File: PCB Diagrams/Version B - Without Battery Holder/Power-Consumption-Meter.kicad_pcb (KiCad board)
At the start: 2 copper layers, 90 x 96.5 mm, 35 parts, among them J1 Jack_DC, J10 01x02, J11 01x02, J12 01x02, J13 01x02, J2 01x02, J3 01x02, J4 USB_A, J5 Jack_DC, J6 Jack_DC, J7 USB_B_Mini, J8 USB_B_Micro, J9 01x04, SW1 SW_SPDT, SW2 SW_Push, U1 INA219_Module, U2 Display_5641BS

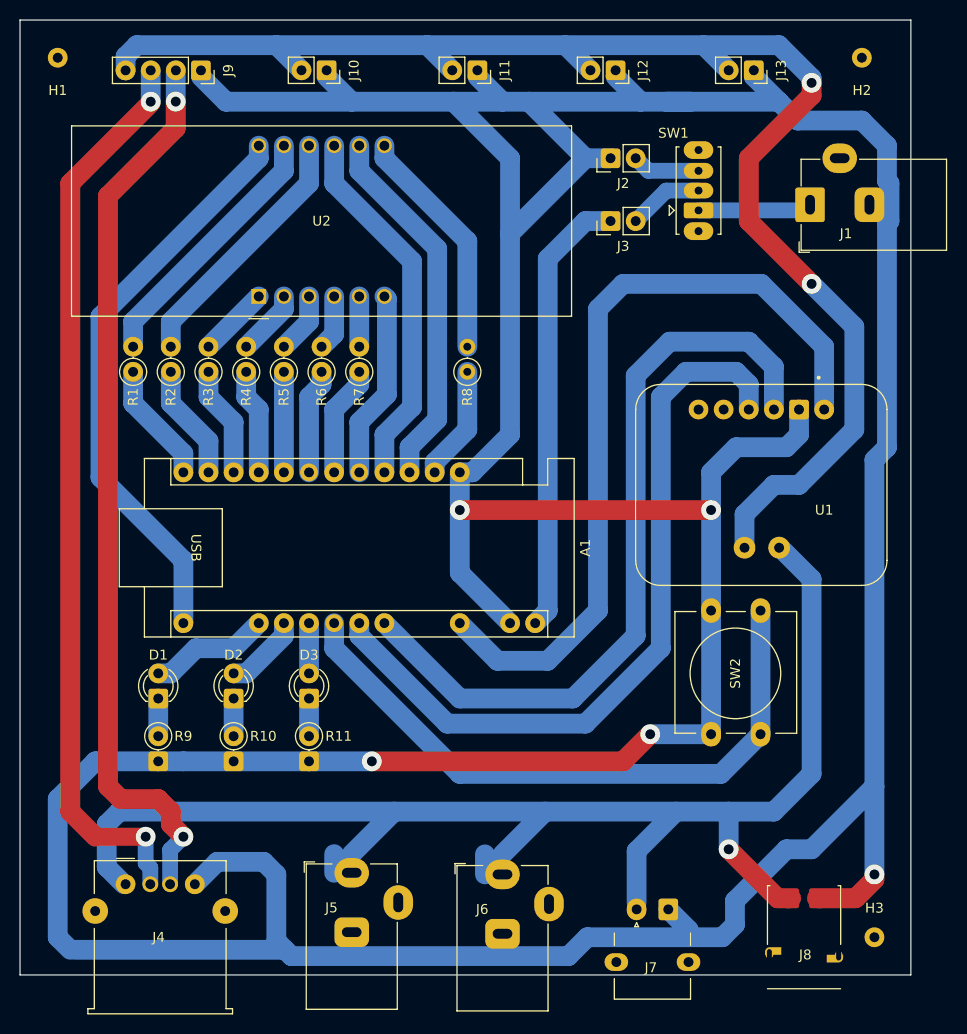
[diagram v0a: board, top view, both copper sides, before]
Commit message: update PCB connectors
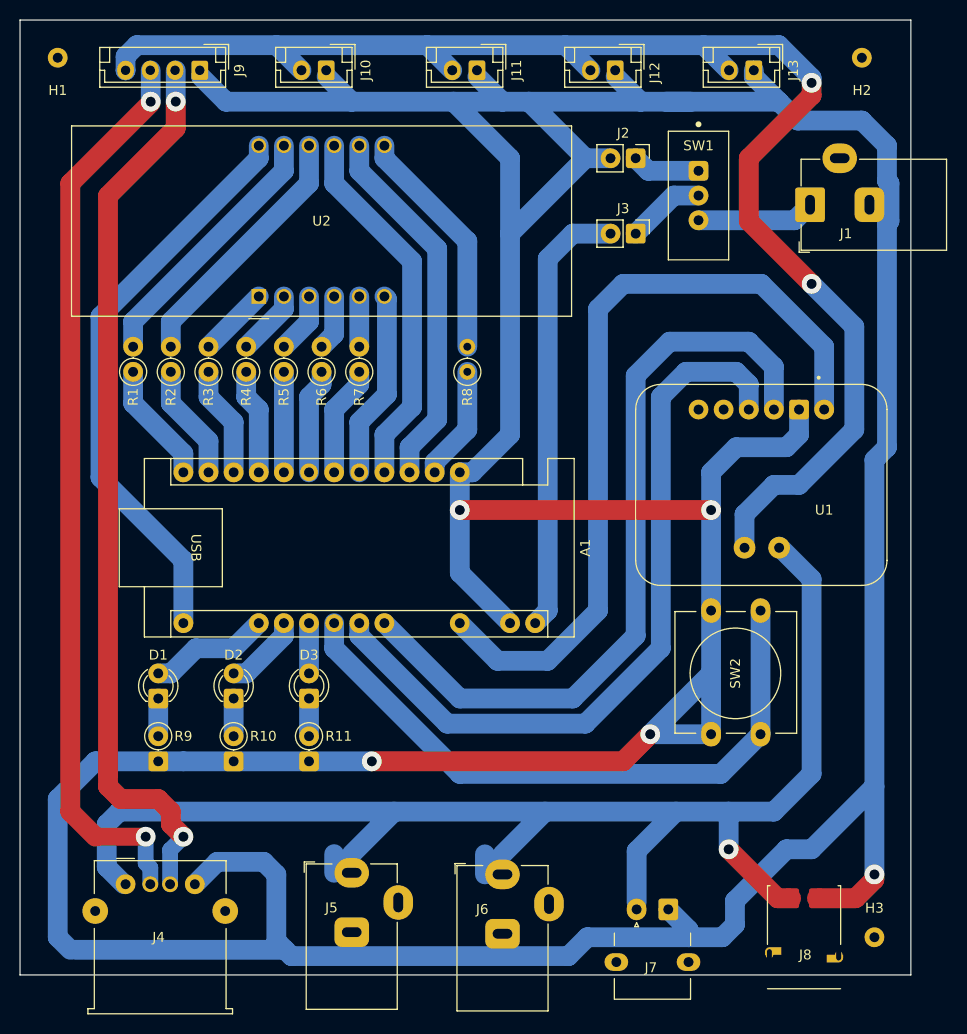
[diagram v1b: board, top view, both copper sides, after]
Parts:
- J10, J11, J12, J13: footprint Connector_PinSocket_2.54mm:PinSocket_1x02_P2.54mm_Vertical -> Connector_JST:JST_EH_B2B-EH-A_1x02_P2.50mm_Vertical
- J2: value 01x02 -> BAT_IN
- J3: value 01x02 -> PWR_BTN
- J9: footprint Connector_PinSocket_2.54mm:PinSocket_1x04_P2.54mm_Vertical -> Connector_JST:JST_EH_B4B-EH-A_1x04_P2.50mm_Vertical
- SW1: value SW_SPDT -> SW_Slide; footprint Button_Switch_THT:SW_Slide_SPDT_Straight_CK_OS102011MS2Q -> Custom:Switch_Slide_SPDT_Straight_TE_1825159_1
- moved J3 2.84 mm to (158.8, 54.6), turned to -90 degrees
- moved J2 2.54 mm to (158.7, 47.0), turned to -90 degrees
- moved SW1 1.50 mm to (165.1, 50.8), turned to -90 degrees
- moved J9 0.12 mm to (114.7, 38.1), turned to 180 degrees
- turned J10 to 180 degrees
- turned J11 to 180 degrees
- turned J12 to 180 degrees
- turned J13 to 180 degrees
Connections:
- J1 pad 1: Net-(SW1-A) -> Net-(J1-Pad1)
- J2 pad 1: GND -> Net-(J2-Pin_1)
- J2 pad 2: Net-(J2-Pin_2) -> GND
- J3 pad 1: PWR -> Net-(J3-Pin_1)
- J3 pad 2: Net-(J3-Pin_2) -> PWR
- SW1 pad 1: Net-(SW1-A) -> Net-(J2-Pin_1)
- SW1 pad 2: Net-(J3-Pin_2) -> Net-(J3-Pin_1)
- SW1 pad 3: Net-(J2-Pin_2) -> Net-(J1-Pad1)
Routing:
- net Net-(J1-Pad1): track 0.00 -> 11.9 mm
- net Net-(SW1-A): track 11.5 -> 0.00 mm
- net GND: track 513.0 -> 521.7 mm
- net Net-(J3-Pin_1): track 0.00 -> 7.94 mm
- net Net-(J3-Pin_2): track 7.63 -> 0.00 mm
- net Net-(J2-Pin_1): track 0.00 -> 6.88 mm
- net Net-(J2-Pin_2): track 6.88 -> 0.00 mm
- net PWR: track 45.3 -> 44.8 mm

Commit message: Adding PCB building and assembly pictures
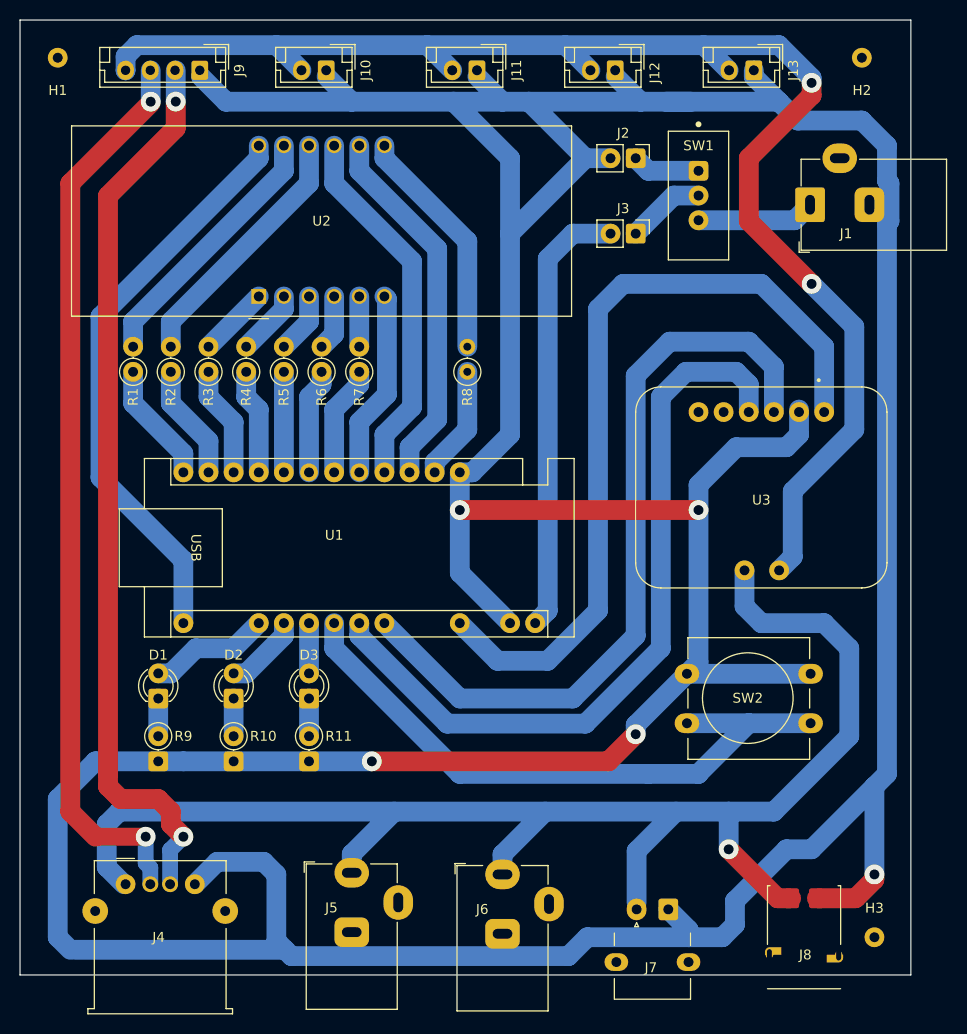
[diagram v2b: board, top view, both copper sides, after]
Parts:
- removed the U1 at (171.4, 80.0)
- added U3: INA219_Module, Custom:INA219_Module_Generic, F.Cu at (171.4, 80.3)
- moved SW2 12.5 mm to (176.4, 104.1), turned to 180 degrees
- renumbered A1 to U1
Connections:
- R2 pad 1: SEG_B -> SEG_F
- R8 pad 1: SEG_F -> SEG_B
- U1 pad 14: SEG_B -> SEG_F
- U1 pad 5: SEG_F -> SEG_B
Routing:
- net VIN+: track 143.6 -> 149.6 mm
- net GND: track 521.7 -> 519.8 mm
- net Net-(U1-A3): track 65.1 -> 64.4 mm
- net VIN-: track 147.6 -> 147.0 mm
